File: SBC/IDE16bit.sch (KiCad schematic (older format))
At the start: 8 parts, among them P1 IDE0, U19 74LS574, U20 74LS574, U21 74HC245

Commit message: Preparation for Pluto v3.0
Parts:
- removed R7: 1K, Resistors_ThroughHole:R_Axial_DIN0411_L9.9mm_D3.6mm_P12.70mm_Horizontal, symbol pluto-rescue:R
- removed U19, U20: 74LS574, Housings_DIP:DIP-20_W7.62mm_Socket, symbol pluto-rescue:74LS574
- removed U21: 74HC245, Housings_DIP:DIP-20_W7.62mm_Socket, symbol pluto-rescue:74HC245
- added C7, C8: 0.1uF, Capacitor_THT:C_Disc_D4.7mm_W2.5mm_P5.00mm, symbol Device:C_Small
- added D2: DIRQ1, Diode_THT:D_T-1_P5.08mm_Horizontal, symbol Device:D_Schottky_Small
- added D4: DIRQ2, Diode_THT:D_T-1_P5.08mm_Horizontal, symbol Device:D_Schottky_Small
- added J12: VIA2PB, Connector_IDC:IDC-Header_2x07_P2.54mm_Vertical, symbol Connector_Generic:Conn_02x07_Odd_Even
- added U7, U9: WD65C22PLCC44, Package_LCC:PLCC-44_THT-Socket, symbol Grotto:WD65C22PLCC44
- P1: footprint Connectors_IDC:IDC-Header_2x20_Pitch2.54mm_Straight -> Connector_IDC:IDC-Header_2x20_P2.54mm_Vertical; symbol conn:CONN_02X20 -> pluto-rescue:CONN_02X20-conn
- R6, R8: footprint Resistors_ThroughHole:R_Axial_DIN0411_L9.9mm_D3.6mm_P12.70mm_Horizontal -> Resistor_THT:R_Axial_DIN0411_L9.9mm_D3.6mm_P7.62mm_Vertical
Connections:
- net labels added: A3, CLK, IDE-A0, IDE-A1, IDE-A2, R-~W, ~IDE-CS0, ~IDE-CS1, ~IDE-DASP, ~IDE-DMACK, ~IDE-RES, ~VIA1SEL, ~VIA2SEL
- net labels removed: DIOR, DIOW, FROM_CLK, FROM_OE, IDE_CS0, OBT_DIR, OBT_OE, TO_CLK, TO_OE, ~IDE:CS0, ~IDE:CS1, ~IDE:DASP, ~IDE:DMACK
- wire segments 108 -> 146
- no-connect marks 5 -> 11
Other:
- note added: "VIA1"
- note added: "VIA2"
- note removed: "High byte from IDE\n"
- note removed: "High byte to IDE"
- moved on the sheet: D3, R6, R8

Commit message: A better layout of PCB.
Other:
- note added: "VIA1 ($7FC0)"
- note added: "VIA2 ($7FA0)"
- note removed: "VIA1"
- note removed: "VIA2"
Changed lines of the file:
@@
 Wire Bus Line
 	4075 5550 6300 5550
-Text Notes 5200 2675 1    60   ~ 12
-VIA1
-Text Notes 10625 2600 1    60   ~ 12
-VIA2
+Text Notes 5225 2850 1    60   ~ 12
+VIA1 ($7FC0)
+Text Notes 10625 2775 1    60   ~ 12
+VIA2 ($7FA0)
 Entry Wire Line
 	11600 1900 11700 1800

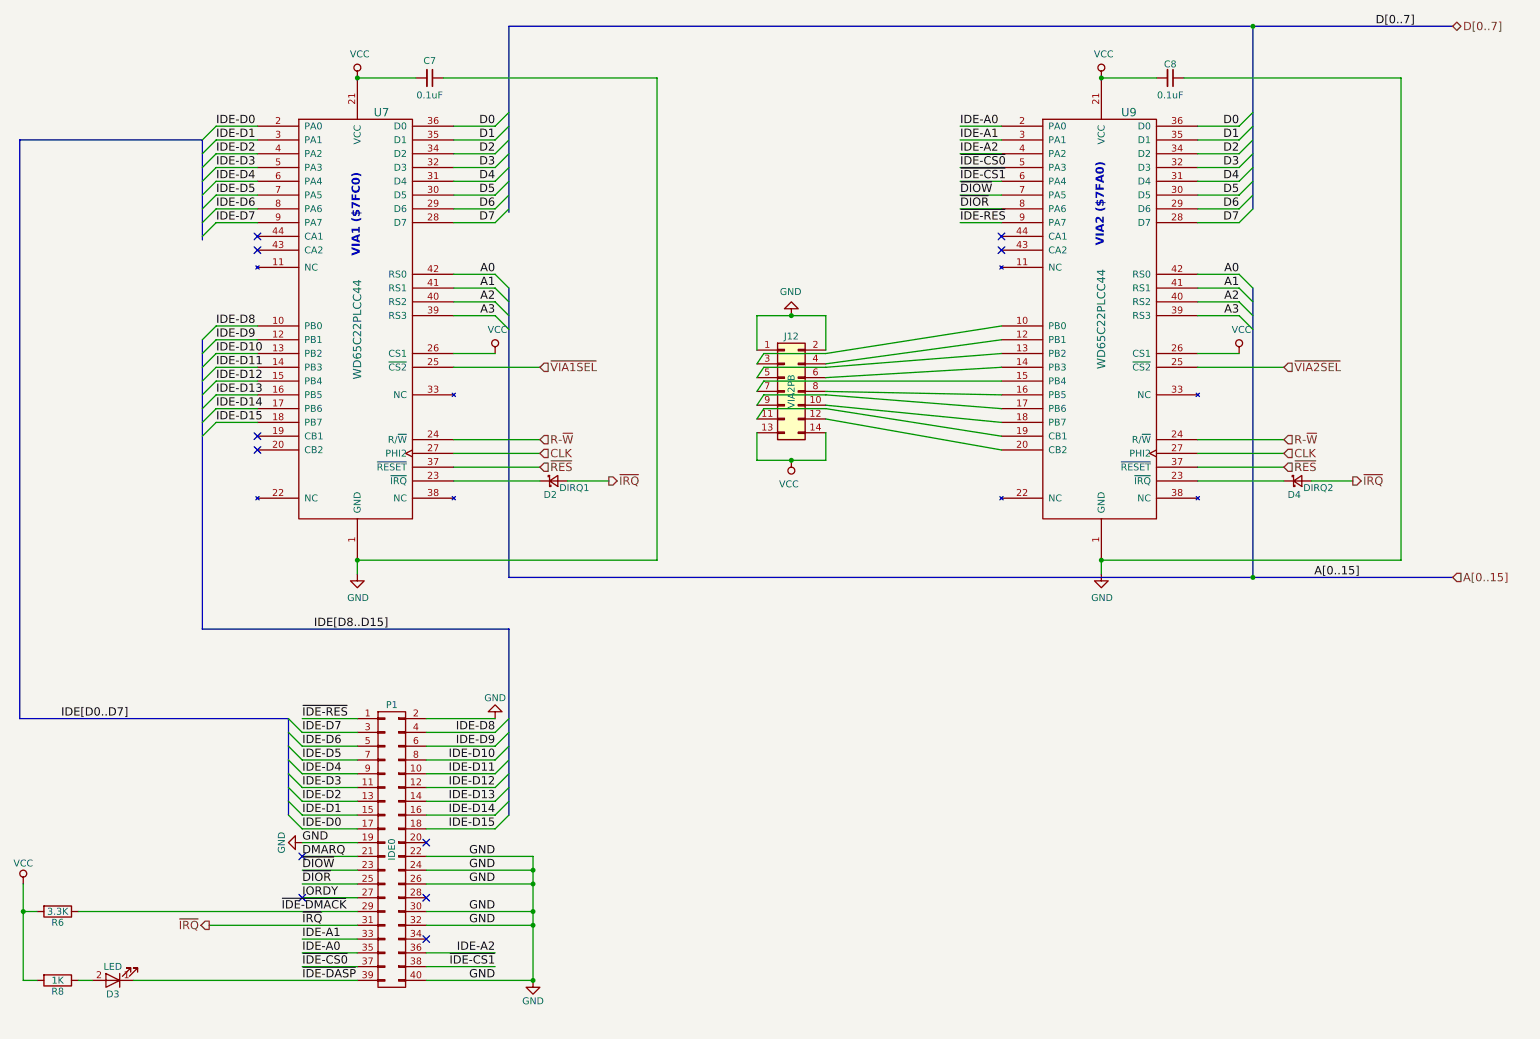
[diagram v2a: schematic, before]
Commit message: Converting to SMD of almost all components.
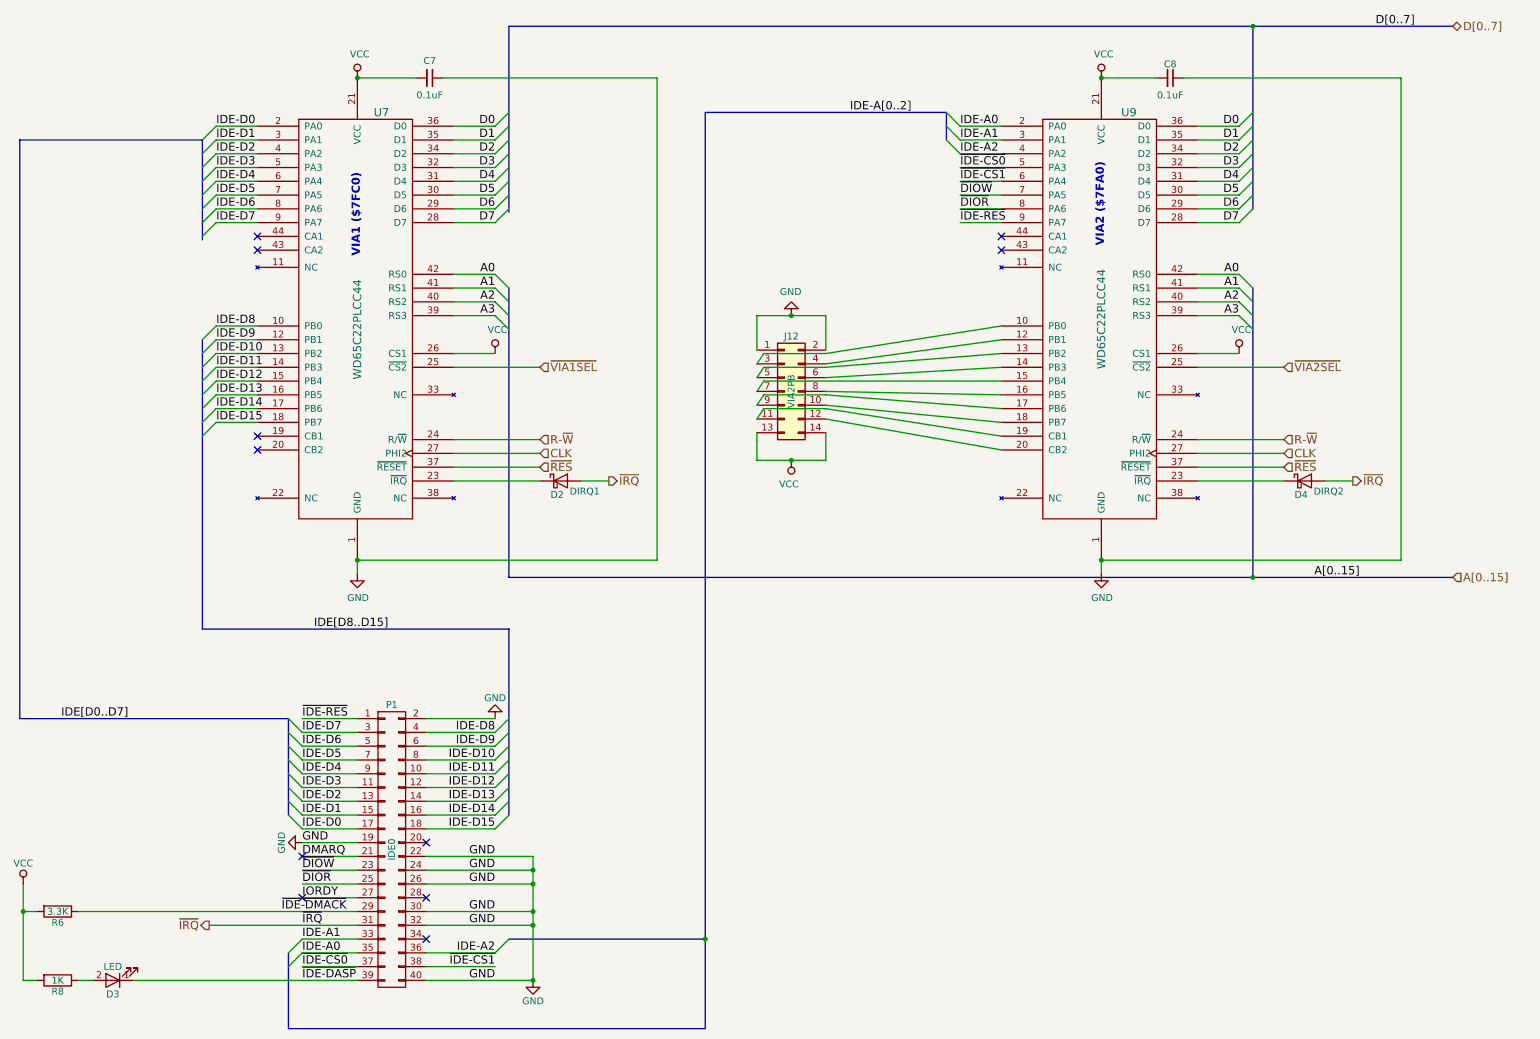
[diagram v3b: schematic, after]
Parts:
- removed D2: DIRQ1, Diode_THT:D_T-1_P5.08mm_Horizontal, symbol Device:D_Schottky_Small
- removed D4: DIRQ2, Diode_THT:D_T-1_P5.08mm_Horizontal, symbol Device:D_Schottky_Small
- added D2: DIRQ1, Diode_SMD:D_SOD-323, symbol Diode:BAT48JFILM
- added D4: DIRQ2, Diode_SMD:D_SOD-323, symbol Diode:BAT48JFILM
- C7, C8: footprint Capacitor_THT:C_Disc_D4.7mm_W2.5mm_P5.00mm -> Capacitor_SMD:C_0603_1608Metric_Pad1.05x0.95mm_HandSolder
- R6, R8: footprint Resistor_THT:R_Axial_DIN0411_L9.9mm_D3.6mm_P7.62mm_Vertical -> Resistor_SMD:R_1206_3216Metric_Pad1.42x1.75mm_HandSolder
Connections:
- net ~IRQ: now also D2.2 (A), D4.2 (A)
- net at U7.23 (~IRQ): now also D2.1 (K)
- net at U9.23 (~IRQ): now also D4.1 (K)
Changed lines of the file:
@@
 F 0 "R8" V 3105 8100 50  0000 C CNN
 F 1 "1K" V 3025 8100 50  0000 C CNN
-F 2 "Resistor_THT:R_Axial_DIN0411_L9.9mm_D3.6mm_P7.62mm_Vertical" V 2955 8100 50  0001 C CNN
+F 2 "Resistor_SMD:R_1206_3216Metric_Pad1.42x1.75mm_HandSolder" V 2955 8100 50  0001 C CNN
 F 3 "" H 3025 8100 50  0000 C CNN
 	1    3025 8100
@@
 F 0 "R6" V 3105 7600 50  0000 C CNN
 F 1 "3.3K" V 3025 7600 50  0000 C CNN
-F 2 "Resistor_THT:R_Axial_DIN0411_L9.9mm_D3.6mm_P7.62mm_Vertical" V 2955 7600 50  0001 C CNN
+F 2 "Resistor_SMD:R_1206_3216Metric_Pad1.42x1.75mm_HandSolder" V 2955 7600 50  0001 C CNN
 F 3 "" H 3025 7600 50  0000 C CNN
 	1    3025 7600
@@
 Text HLabel 13150 5175 2    60   Input ~ 0
 A[0..15]
-$Comp
-L Device:D_Schottky_Small D2
-U 1 1 5D4C1216
-P 6625 4475
-F 0 "D2" H 6600 4375 50  0000 C CNN
-F 1 "DIRQ1" H 6775 4425 50  0000 C CNN
-F 2 "Diode_THT:D_T-1_P5.08mm_Horizontal" V 6625 4475 50  0001 C CNN
-F 3 "~" V 6625 4475 50  0001 C CNN
-	1    6625 4475
-	1    0    0    -1
-$EndComp
-$Comp
-L Device:D_Schottky_Small D4
-U 1 1 5D4C1BC7
-P 12025 4475
-F 0 "D4" H 12000 4375 50  0000 C CNN
-F 1 "DIRQ2" H 12175 4425 50  0000 C CNN
-F 2 "Diode_THT:D_T-1_P5.08mm_Horizontal" V 12025 4475 50  0001 C CNN
-F 3 "~" V 12025 4475 50  0001 C CNN
-	1    12025 4475
-	1    0    0    -1
-$EndComp
-Wire Wire Line
-	12125 4475 12425 4475
-Wire Wire Line
-	6725 4475 7025 4475
+Wire Wire Line
+	12225 4475 12425 4475
+Wire Wire Line
+	6825 4475 7025 4475
 Text HLabel 7025 4475 2    60   Output ~ 0
 ~IRQ
@@
 F 0 "C7" V 5600 1550 50  0000 C CNN
 F 1 "0.1uF" V 5850 1550 50  0000 C CNN
-F 2 "Capacitor_THT:C_Disc_D4.7mm_W2.5mm_P5.00mm" H 5725 1550 50  0001 C CNN
+F 2 "Capacitor_SMD:C_0603_1608Metric_Pad1.05x0.95mm_HandSolder" H 5725 1550 50  0001 C CNN
 F 3 "~" H 5725 1550 50  0001 C CNN
 	1    5725 1550
@@
 F 0 "C8" V 11000 1550 50  0000 C CNN
 F 1 "0.1uF" V 11225 1550 50  0000 C CNN
-F 2 "Capacitor_THT:C_Disc_D4.7mm_W2.5mm_P5.00mm" H 11100 1550 50  0001 C CNN
+F 2 "Capacitor_SMD:C_0603_1608Metric_Pad1.05x0.95mm_HandSolder" H 11100 1550 50  0001 C CNN
 F 3 "~" H 11100 1550 50  0001 C CNN
 	1    11100 1550
@@
 Wire Wire Line
 	3575 8100 5200 8100
+Entry Wire Line
+	9475 1800 9575 1900
+Entry Wire Line
+	9475 1900 9575 2000
+Entry Wire Line
+	9475 2000 9575 2100
+Text Label 8775 1800 0    60   ~ 0
+IDE-A[0..2]
+Entry Wire Line
+	6200 7900 6300 7800
+Wire Bus Line
+	7725 1800 9475 1800
+Entry Wire Line
+	4700 7900 4800 7800
+Entry Wire Line
+	4700 8000 4800 7900
+Wire Bus Line
+	4700 8450 7725 8450
+Wire Bus Line
+	7725 1800 7725 7800
+Wire Bus Line
+	6300 7800 7725 7800
+Connection ~ 7725 7800
+Wire Bus Line
+	7725 7800 7725 8450
+$Comp
+L Diode:BAT48JFILM D4
+U 1 1 5D6C1D60
+P 12075 4475
+F 0 "D4" H 12050 4375 50  0000 C CNN
+F 1 "DIRQ2" H 12250 4400 50  0000 C CNN
+F 2 "Diode_SMD:D_SOD-323" H 12075 4300 50  0001 C CNN
+F 3 "www.st.com/resource/en/datasheet/bat48.pdf" H 12075 4475 50  0001 C CNN
+	1    12075 4475
+	1    0    0    -1
+$EndComp
+$Comp
+L Diode:BAT48JFILM D2
+U 1 1 5D6D7B96
+P 6675 4475
+F 0 "D2" H 6650 4375 50  0000 C CNN
+F 1 "DIRQ1" H 6850 4400 50  0000 C CNN
+F 2 "Diode_SMD:D_SOD-323" H 6675 4300 50  0001 C CNN
+F 3 "www.st.com/resource/en/datasheet/bat48.pdf" H 6675 4475 50  0001 C CNN
+	1    6675 4475
+	1    0    0    -1
+$EndComp
+Wire Bus Line
+	9475 1800 9475 2000
+Wire Bus Line
+	4700 7900 4700 8450
 Wire Bus Line
 	11700 3075 11700 5175

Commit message: New PCB layout is taking shape.
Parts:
- C7, C8: footprint Capacitor_SMD:C_0603_1608Metric_Pad1.05x0.95mm_HandSolder -> Capacitor_SMD:C_0805_2012Metric_Pad1.15x1.40mm_HandSolder
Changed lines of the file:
@@
 F 0 "C7" V 5600 1550 50  0000 C CNN
 F 1 "0.1uF" V 5850 1550 50  0000 C CNN
-F 2 "Capacitor_SMD:C_0603_1608Metric_Pad1.05x0.95mm_HandSolder" H 5725 1550 50  0001 C CNN
+F 2 "Capacitor_SMD:C_0805_2012Metric_Pad1.15x1.40mm_HandSolder" H 5725 1550 50  0001 C CNN
 F 3 "~" H 5725 1550 50  0001 C CNN
 	1    5725 1550
@@
 F 0 "C8" V 11000 1550 50  0000 C CNN
 F 1 "0.1uF" V 11225 1550 50  0000 C CNN
-F 2 "Capacitor_SMD:C_0603_1608Metric_Pad1.05x0.95mm_HandSolder" H 11100 1550 50  0001 C CNN
+F 2 "Capacitor_SMD:C_0805_2012Metric_Pad1.15x1.40mm_HandSolder" H 11100 1550 50  0001 C CNN
 F 3 "~" H 11100 1550 50  0001 C CNN
 	1    11100 1550

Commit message: Pluto2 V3 PCB routed and finished. Removed all Pluto2 V2 Gerber files. Add GAL files for address and IO decoding.
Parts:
- D2, D4: footprint Diode_SMD:D_SOD-323 -> Diode_SMD:D_SOD-323_HandSoldering
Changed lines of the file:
@@
 	5200 7200 4800 7200
 Wire Wire Line
-	5200 7300 4800 7300
-Wire Wire Line
-	5200 7400 4800 7400
-Wire Wire Line
 	5200 7500 4800 7500
 Wire Wire Line
 	5200 7800 4800 7800
 Wire Wire Line
-	5200 8000 4800 8000
-Wire Wire Line
 	5700 6300 6200 6300
 Wire Wire Line
@@
 Wire Wire Line
 	5700 7900 6200 7900
-Wire Wire Line
-	5700 8000 6200 8000
 Wire Wire Line
 	6475 8100 5700 8100
@@
 Wire Wire Line
 	9875 2100 9575 2100
-Wire Wire Line
-	9875 2200 9575 2200
-Wire Wire Line
-	9875 2300 9575 2300
-Wire Wire Line
-	9875 2400 9575 2400
-Wire Wire Line
-	9875 2500 9575 2500
-Wire Wire Line
-	9875 2600 9575 2600
 Wire Wire Line
 	9875 3650 8600 3725
@@
 F 0 "D4" H 12050 4375 50  0000 C CNN
 F 1 "DIRQ2" H 12250 4400 50  0000 C CNN
-F 2 "Diode_SMD:D_SOD-323" H 12075 4300 50  0001 C CNN
+F 2 "Diode_SMD:D_SOD-323_HandSoldering" H 12075 4300 50  0001 C CNN
 F 3 "www.st.com/resource/en/datasheet/bat48.pdf" H 12075 4475 50  0001 C CNN
 	1    12075 4475
@@
 F 0 "D2" H 6650 4375 50  0000 C CNN
 F 1 "DIRQ1" H 6850 4400 50  0000 C CNN
-F 2 "Diode_SMD:D_SOD-323" H 6675 4300 50  0001 C CNN
+F 2 "Diode_SMD:D_SOD-323_HandSoldering" H 6675 4300 50  0001 C CNN
 F 3 "www.st.com/resource/en/datasheet/bat48.pdf" H 6675 4475 50  0001 C CNN
 	1    6675 4475
 	1    0    0    -1
 $EndComp
+Wire Wire Line
+	7500 2200 7500 5700
+Wire Wire Line
+	7500 5700 4250 5700
+Wire Wire Line
+	4250 5700 4250 8000
+Wire Wire Line
+	7500 2200 9875 2200
+Wire Wire Line
+	8000 2300 8000 8000
+Wire Wire Line
+	5700 8000 8000 8000
+Wire Wire Line
+	8000 2300 9875 2300
+Wire Wire Line
+	7575 2500 7575 5800
+Wire Wire Line
+	7575 5800 4350 5800
+Wire Wire Line
+	4350 5800 4350 7400
+Wire Wire Line
+	4350 7400 5200 7400
+Wire Wire Line
+	7575 2500 9875 2500
+Wire Wire Line
+	7650 2400 7650 5900
+Wire Wire Line
+	7650 5900 4450 5900
+Wire Wire Line
+	4450 5900 4450 7300
+Wire Wire Line
+	4450 7300 5200 7300
+Wire Wire Line
+	7650 2400 9875 2400
+Wire Wire Line
+	7800 2600 7800 6000
+Wire Wire Line
+	7800 6000 4800 6000
+Wire Wire Line
+	4800 6000 4800 6200
+Wire Wire Line
+	7800 2600 9875 2600
 Wire Bus Line
 	9475 1800 9475 2000
 Wire Bus Line
 	4700 7900 4700 8450
+Wire Wire Line
+	4250 8000 5200 8000
 Wire Bus Line
 	11700 3075 11700 5175
